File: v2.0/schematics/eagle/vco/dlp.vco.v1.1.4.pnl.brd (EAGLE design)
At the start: 73.3 x 49.5 mm, 26 parts, among them J1 PWM IN1, J2 EXP.IN1, J3 EXP.IN2, J4 OSC OUT1, J5 CV.IN, SW1 50K (log), SW2 50K (log)

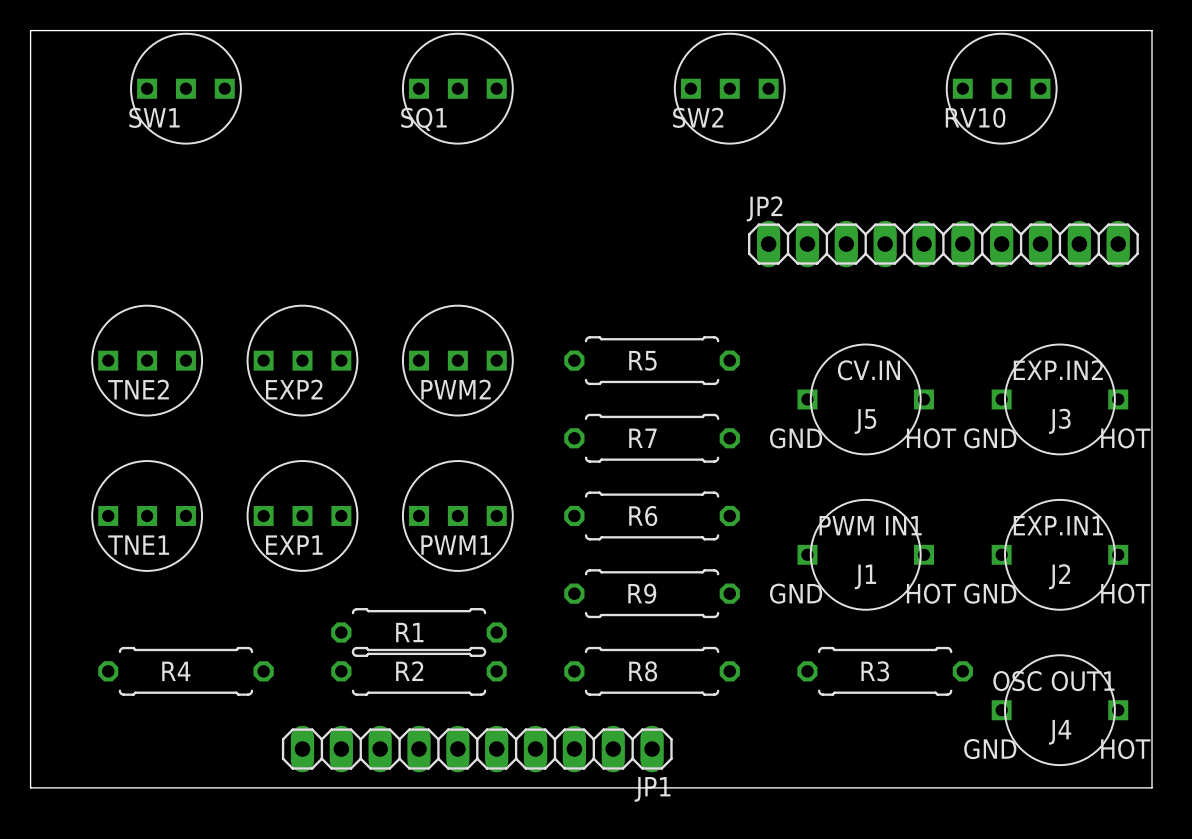
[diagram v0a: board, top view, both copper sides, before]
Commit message: Reduced size of vco pannel and applied routing
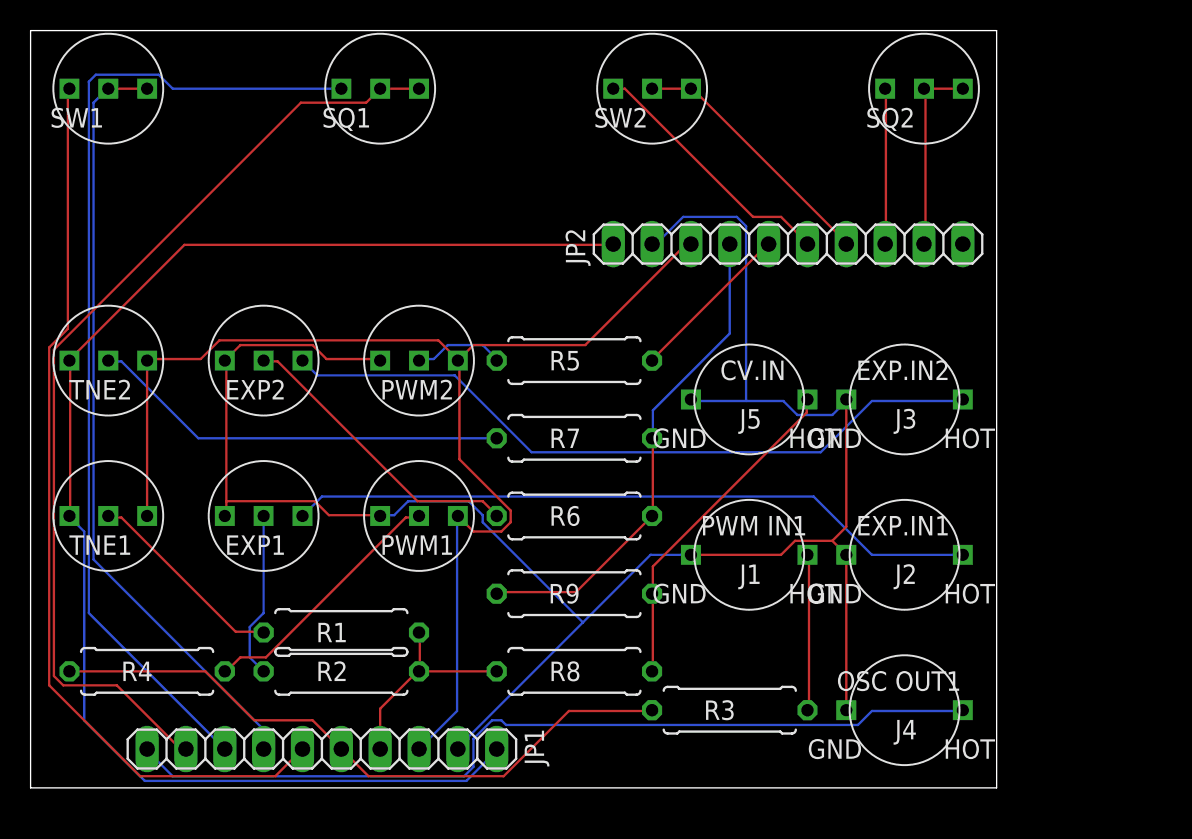
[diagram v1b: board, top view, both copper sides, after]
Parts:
- removed RV10: 50K (log), _common:R-VAR
- added SQ2: 50K (log), _common:R-VAR
- moved R3 10.5 mm to (45.7, 5.08)
- moved J2 10.2 mm to (57.1, 15.2)
- moved J3 10.2 mm to (57.1, 25.4)
- moved J4 10.2 mm to (57.1, 5.08)
- moved JP1 10.2 mm to (19.1, 2.54)
- moved JP2 10.2 mm to (49.5, 35.6)
- moved J1 7.62 mm to (47.0, 15.2)
- moved J5 7.62 mm to (47.0, 25.4)
- moved SQ1 5.08 mm to (22.9, 45.7)
- moved SW1 5.08 mm to (5.08, 45.7)
- moved R1 5.08 mm to (20.3, 10.2)
- moved R2 5.08 mm to (20.3, 7.62)
- moved R5 5.08 mm to (35.6, 27.9)
- moved R6 5.08 mm to (35.6, 17.8)
- moved R7 5.08 mm to (35.6, 22.9)
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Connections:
- net N$PNL.SQ.LVL2A: now also SQ2.R1; no longer RV10.R1
- net N$PNL.SQ.LVL2B: now also SQ2.R2, SQ2.VAR; no longer RV10.R2, RV10.VAR
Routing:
- net N$PNL.0V: track 0.00 -> 130.0 mm
- net N$PNL.N12V: track 0.00 -> 92.3 mm
- net N$PNL.P12V: track 0.00 -> 82.5 mm
- net N$PNL.SQ.LVL1A: track 0.00 -> 64.4 mm
- net N$PNL.SQ.LVL1B: track 0.00 -> 62.9 mm
- net N$PNL.SW.LVL1A: track 0.00 -> 59.4 mm
- net N$PNL.OSC.OUT1: track 0.00 -> 57.3 mm
- net N$PNL.SW.LVL1B: track 0.00 -> 50.8 mm
- net N$6: track 0.00 -> 47.2 mm
- net N$4: track 0.00 -> 45.3 mm
- net N$PNL.PWM1: track 0.00 -> 42.7 mm
- net N$PNL.EXP2: track 0.00 -> 32.3 mm
- net N$3: track 0.00 -> 27.5 mm
- net N$1: track 0.00 -> 22.0 mm
- net N$5: track 0.00 -> 19.5 mm
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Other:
- board size 73.3 x 49.5 mm -> 63.2 x 49.5 mm
